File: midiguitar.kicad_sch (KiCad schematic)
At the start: 14 parts

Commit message: Refactor code structure for improved readability and maintainability
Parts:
- removed Q?: Transistor_MOSFET_NCh_SOT23, PCM_fab:SOT-23-3, symbol PCM_fab:Transistor_MOSFET_NCh_SOT23
- removed U?: Sensor_IMU_ST_LSM6DSV16XTR, PCM_fab:Sensor_IMU_ST_LSM6DSV16XTR, symbol PCM_fab:Sensor_IMU_ST_LSM6DSV16XTR
- removed U?: ZC440600, ZC440600:MODULE_ZC440600, symbol ZC440600:ZC440600

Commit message: Remove lock files for midiguitar project to clean up workspace
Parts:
- removed P?: Conn_USB_A_Plug, PCM_fab:Conn_USB_A_Plug, symbol PCM_fab:Conn_USB_A_Plug
- removed R? (x3): 10k, PCM_fab:R_1206, symbol PCM_fab:R_1206
- removed SW?: Switch_Slide_Top_CnK, PCM_fab:Switch_Slide_Top_CnK_JS102011SCQN_8.5x3.5mm, symbol PCM_fab:Switch_Slide_Top_CnK
- added J1: ToF VL53L4CD, midiguitar:1X06_NO_SILK, symbol midiguitar-eagle-import:CONN_06NO_SILK_NO_POP
- added J2: ToF VL6180X, midiguitar:1X06_NO_SILK, symbol midiguitar-eagle-import:CONN_06NO_SILK_NO_POP
- added J?: PinHeader_NeoPixel_16Led, PCM_fab:PinSocket_01x03_P2.54mm_Vertical_SMD, symbol PCM_fab:PinSocket_01x03_P2.54mm_Vertical_SMD
- added R2: 10k, PCM_fab:R_1206, symbol PCM_fab:R_1206
- added SW1, SW2: Switch_Slide_1, PCM_fab:Switch_Slide_Top_CnK_JS102011SCQN_8.5x3.5mm, symbol PCM_fab:Switch_Slide_Top_CnK
- added U2: LevelShifter_Texas_TXB0104DR_SOIC-14, PCM_fab:LevelShifter_Texas_TXB0104DR_SOIC-14, symbol PCM_fab:LevelShifter_Texas_TXB0104DR_SOIC-14
- M1: renamed from M?; value Module_XIAO-ESP32S3 -> ESP32S3
- gave numbers to parts that had none: 4
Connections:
- net at R1.1: now also SW1.3 (C)
- net at R1.2: now also M1.2 (D1)
- net at M1.1 (D0): now also U2.2 (A1)
- net PWR_3V3: now reaches M1.12 (3V3)
- net PWR_3V3: now also J1.2, J2.2
- net PWR_5V: now reaches M1.14 (5V)
- net PWR_5V: now also J?.2 (Pin_2), U2.1 (VCCA)
- net at M1.21 (GND): now also J1.1, J2.1, J?.3 (Pin_1), SW1.2 (B), SW2.2 (B), U2.7 (GND)
- net at M1.4 (D3): now also R2.2
- net SDA: now reaches M1.7 (D6)
- net SDA: now also J1.3, J2.3
- net SCL: now reaches M1.8 (D7)
- net SCL: now also J1.4, J2.4
- new net: R2.1, SW2.3 (C)
- new net: J?.1 (Pin_1), U2.14 (VCCB)
- new net ~{INT}: J1.5
- new net ~{SHUT}: J1.6

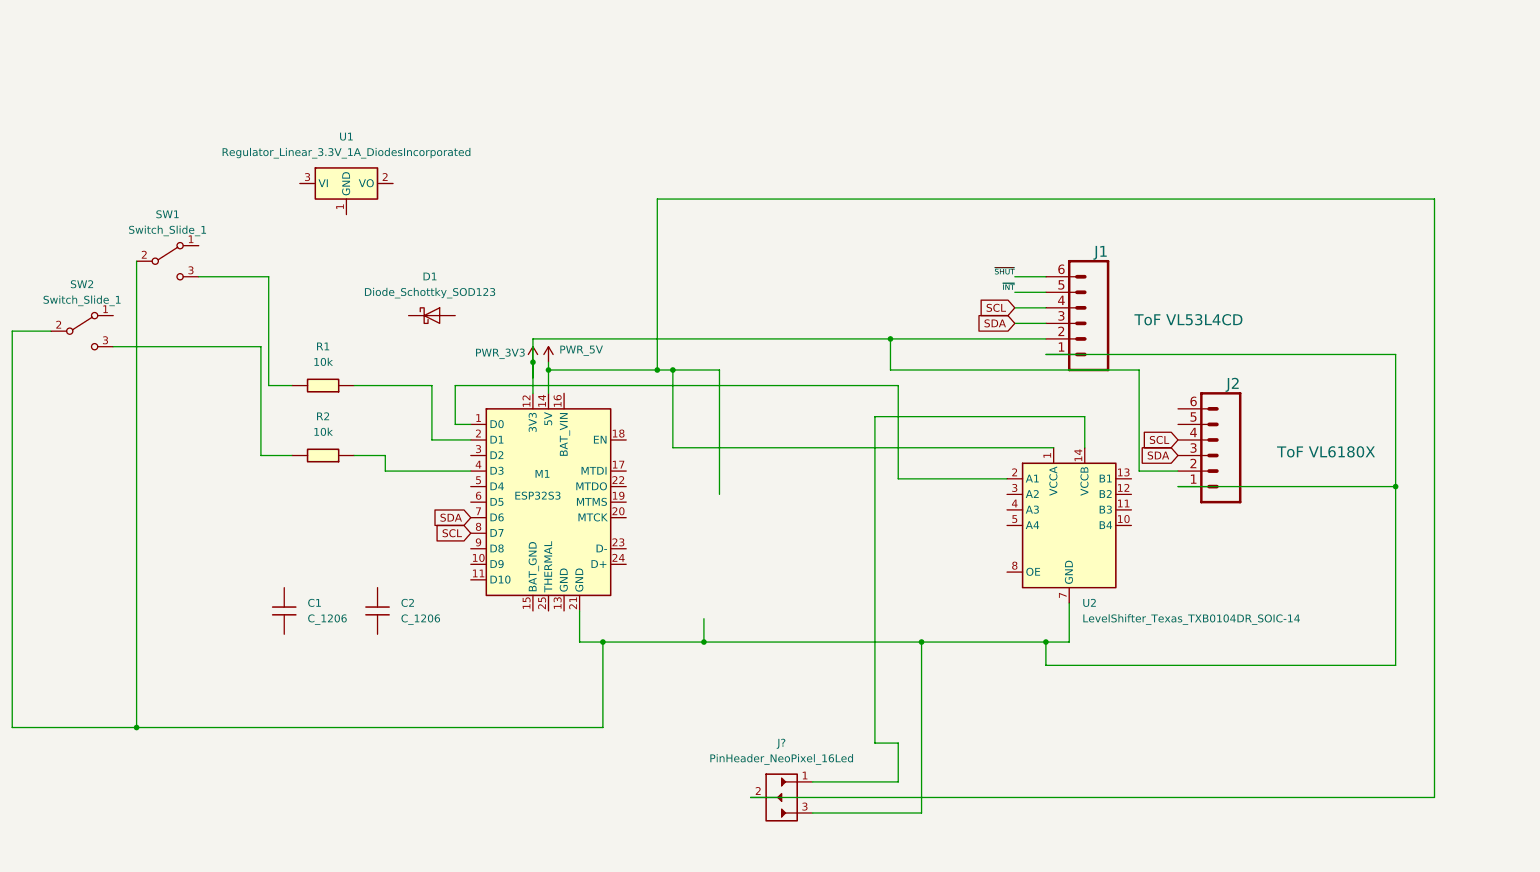
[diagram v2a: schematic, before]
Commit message: Update sym-lib-table version to 7 for midiguitar-eagle-import library
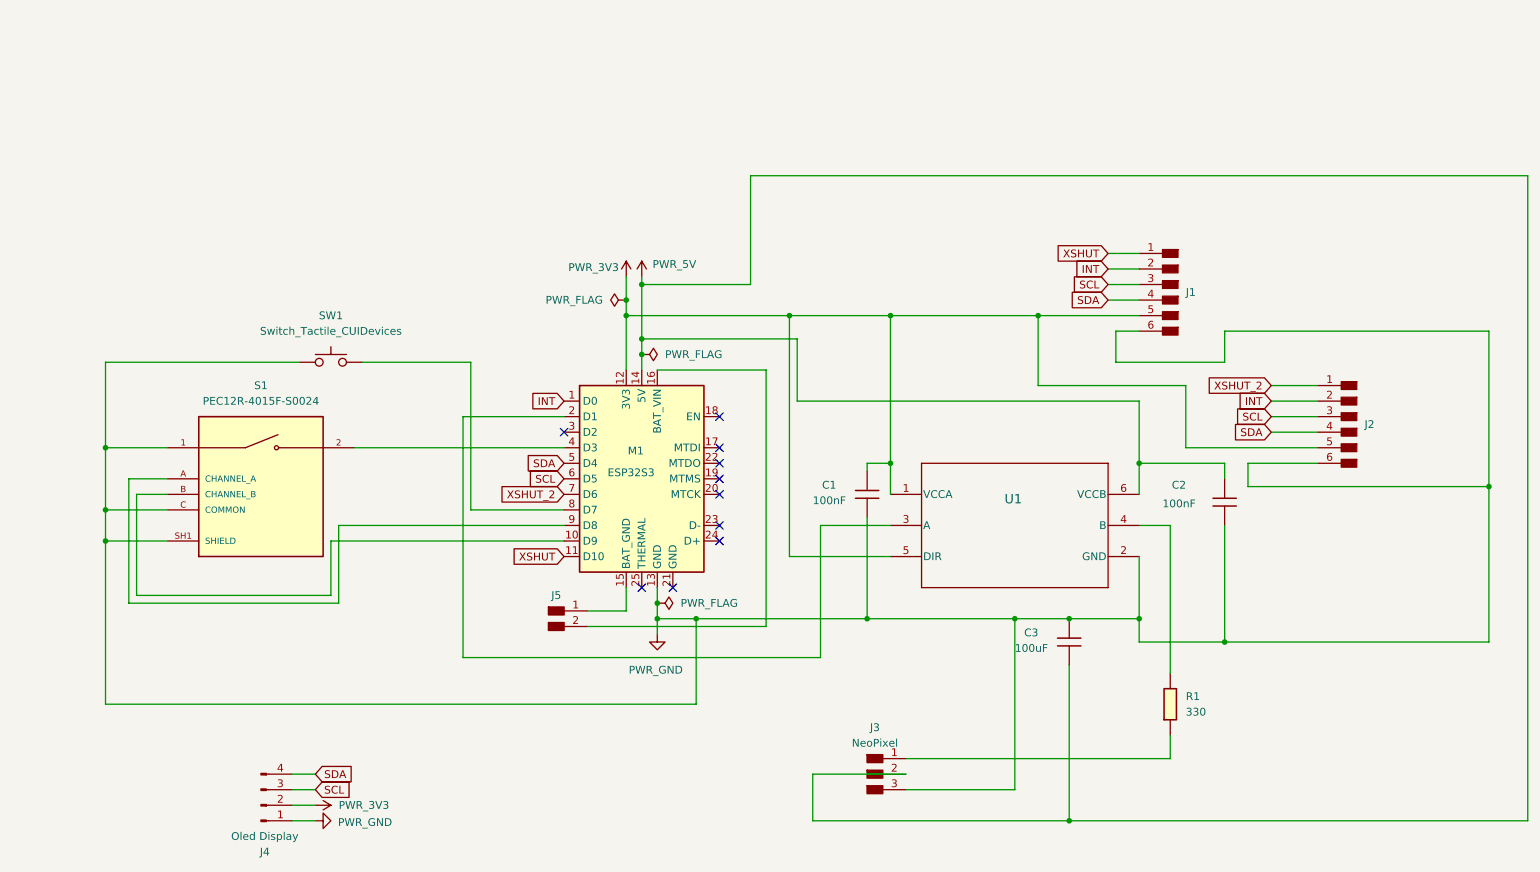
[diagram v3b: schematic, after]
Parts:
- removed D1: Diode_Schottky_SOD123, PCM_fab:Diode_Schottky_SOD123, symbol PCM_fab:Diode_Schottky_SOD123
- removed J1: ToF VL53L4CD, midiguitar:1X06_NO_SILK, symbol midiguitar-eagle-import:CONN_06NO_SILK_NO_POP
- removed J2: ToF VL6180X, midiguitar:1X06_NO_SILK, symbol midiguitar-eagle-import:CONN_06NO_SILK_NO_POP
- removed J?: PinHeader_NeoPixel_16Led, PCM_fab:PinSocket_01x03_P2.54mm_Vertical_SMD, symbol PCM_fab:PinSocket_01x03_P2.54mm_Vertical_SMD
- removed R2: 10k, PCM_fab:R_1206, symbol PCM_fab:R_1206
- removed SW1, SW2: Switch_Slide_1, PCM_fab:Switch_Slide_Top_CnK_JS102011SCQN_8.5x3.5mm, symbol PCM_fab:Switch_Slide_Top_CnK
- removed U1: Regulator_Linear_3.3V_1A_DiodesIncorporated, PCM_fab:SOT-223-3_TabPin2, symbol PCM_fab:Regulator_Linear_3.3V_1A_DiodesIncorporated
- removed U2: LevelShifter_Texas_TXB0104DR_SOIC-14, PCM_fab:LevelShifter_Texas_TXB0104DR_SOIC-14, symbol PCM_fab:LevelShifter_Texas_TXB0104DR_SOIC-14
- added C3: 100uF, PCM_fab:C_1206, symbol PCM_fab:C_1206
- added J1, J2: PinHeader_01x06_P2.54mm_Vertical_THT_D1mm, PCM_fab:PinHeader_01x06_P2.54mm_Vertical_THT_D1mm, symbol PCM_fab:PinHeader_01x06_P2.54mm_Vertical_THT_D1mm
- added J3: NeoPixel, PCM_fab:PinHeader_01x03_P2.54mm_Vertical_THT_D1mm, symbol PCM_fab:PinHeader_01x03_P2.54mm_Vertical_THT_D1mm
- added J4: Oled Display, footprints:Display_128x64_096_I2C, symbol Connector:Conn_01x04_Pin
- added J5: (no value), PCM_fab:PinHeader_01x02_P2.54mm_Vertical_THT_D1mm, symbol PCM_fab:PinHeader_01x02_P2.54mm_Vertical_THT_D1mm
- added S1: PEC12R-4015F-S0024, PEC12R-4015F-S0024:XDCR_PEC12R-4015F-S0024, symbol PEC12R-4015F-S0024:PEC12R-4015F-S0024
- added SW1: Switch_Tactile_CUIDevices, PCM_fab:Button_CUIDevices_TS04-66-43-BK-260-SMT_6.0x6.0mm, symbol PCM_fab:Switch_Tactile_CUIDevices
- added U1: SN74LVC1T45DBVR, DBV0006A_N, symbol 2026-04-11_16-51-34:SN74LVC1T45DBVR
- C1, C2: value C_1206 -> 100nF
- R1: value 10k -> 330
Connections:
- net PWR_3V3: now also C1.1, J1.5 (Pin_5), J2.5 (Pin_5), J4.2 (Pin_2), U1.1 (VCCA), U1.5 (DIR)
- net PWR_5V: now also C2.1, C3.2, J3.2 (Pin_2), U1.6 (VCCB)
- net SCL: now also M1.6 (D5), J1.3 (Pin_3), J2.3 (Pin_3), J4.3 (Pin_3); no longer M1.8 (D7)
- net SDA: now also M1.5 (D4), J1.4 (Pin_4), J2.4 (Pin_4), J4.4 (Pin_4); no longer M1.7 (D6)
- net at M1.4 (D3): now also S1.2
- net PWR_GND: now reaches C1.2
- net PWR_GND: now also C2.2, M1.13 (GND), C3.1, J1.6 (Pin_6), J2.6 (Pin_6), J3.3 (Pin_3), J4.1 (Pin_1), S1.1, S1.C (COMMON), S1.SH1 (SHIELD), S1.SH2 (SHIELD), SW1.1, SW1.2, U1.2 (GND)
- net at R1.1: now also U1.4 (B)
- net at M1.2 (D1): now also U1.3 (A); no longer R1.2
- net INT: now reaches M1.1 (D0)
- net INT: now also J1.2 (Pin_2), J2.2 (Pin_2)
- net at M1.10 (D9): now also S1.B (CHANNEL_B)
- net XSHUT: now reaches M1.11 (D10)
- net XSHUT: now also J1.1 (Pin_1)
- net at M1.15 (BAT_GND): now also J5.1 (Pin_1)
- net at M1.16 (BAT_VIN): now also J5.2 (Pin_2)
- net at M1.9 (D8): now also S1.A (CHANNEL_A)
- new net: M1.8 (D7), SW1.3, SW1.4
- new net: J3.1 (Pin_1), R1.2
- new net XSHUT_2: J2.1 (Pin_1), M1.7 (D6)
- no-connect marks 0 -> 10
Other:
- company: (none) -> Alejandro De Leon
- title: (none) -> MidiGuitar
- moved on the sheet: M1
